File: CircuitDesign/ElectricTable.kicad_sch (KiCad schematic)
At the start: 7 parts

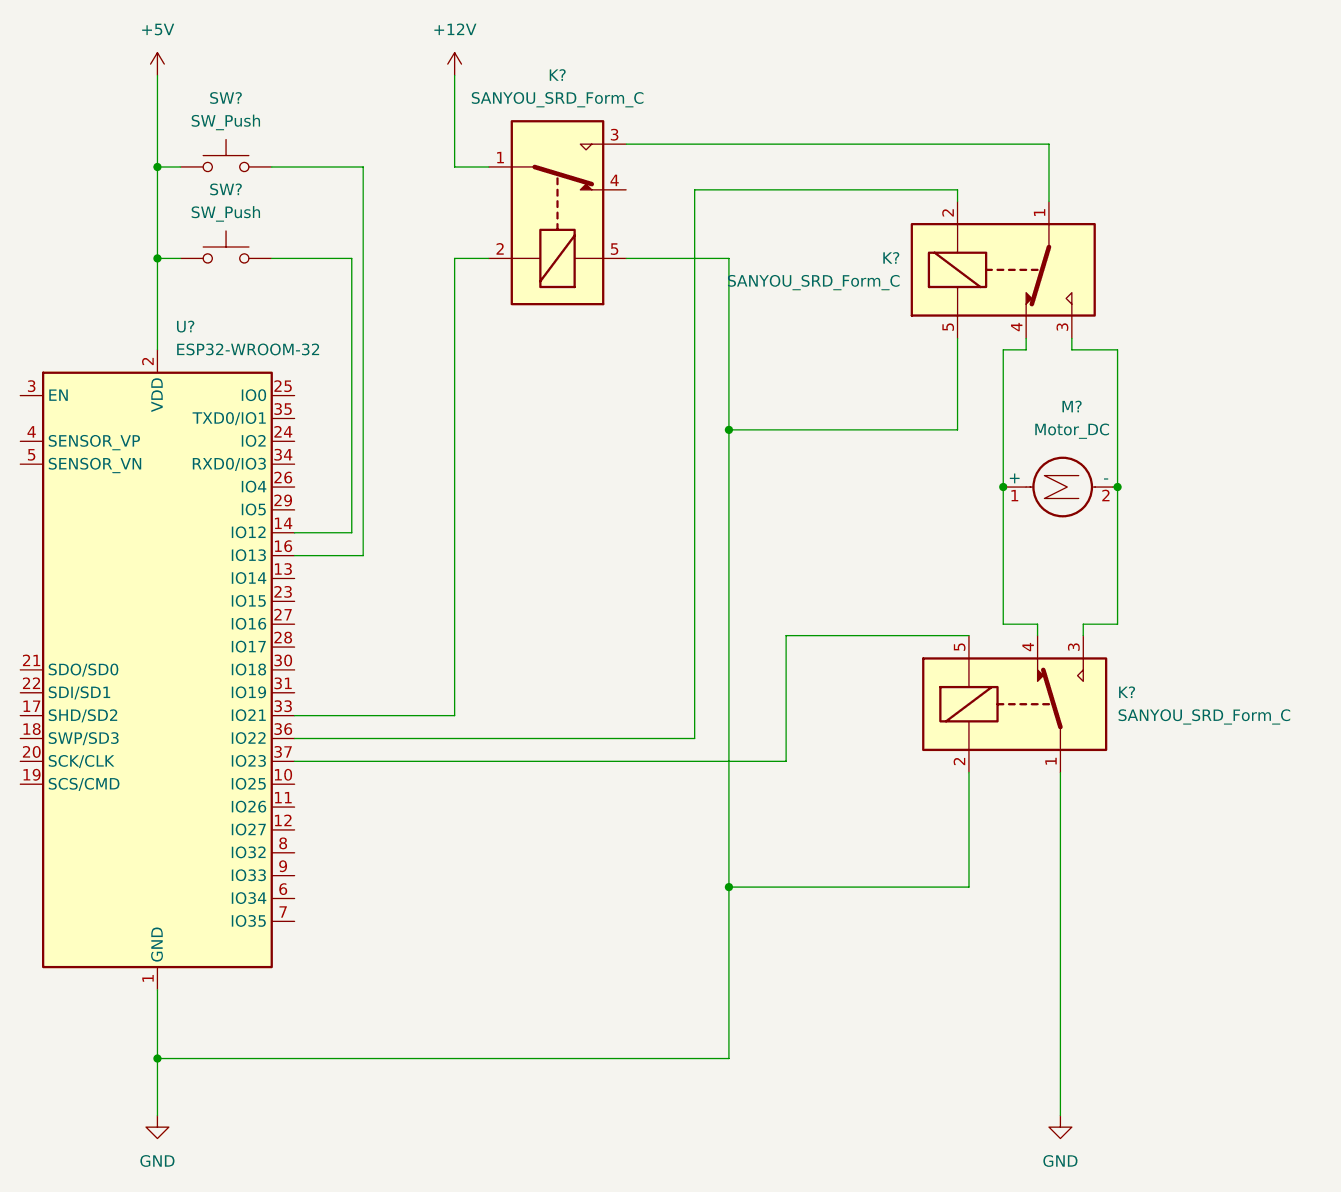
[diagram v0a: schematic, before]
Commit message: Simplified circuit to use dedicated H bridge instead of self made relay solution
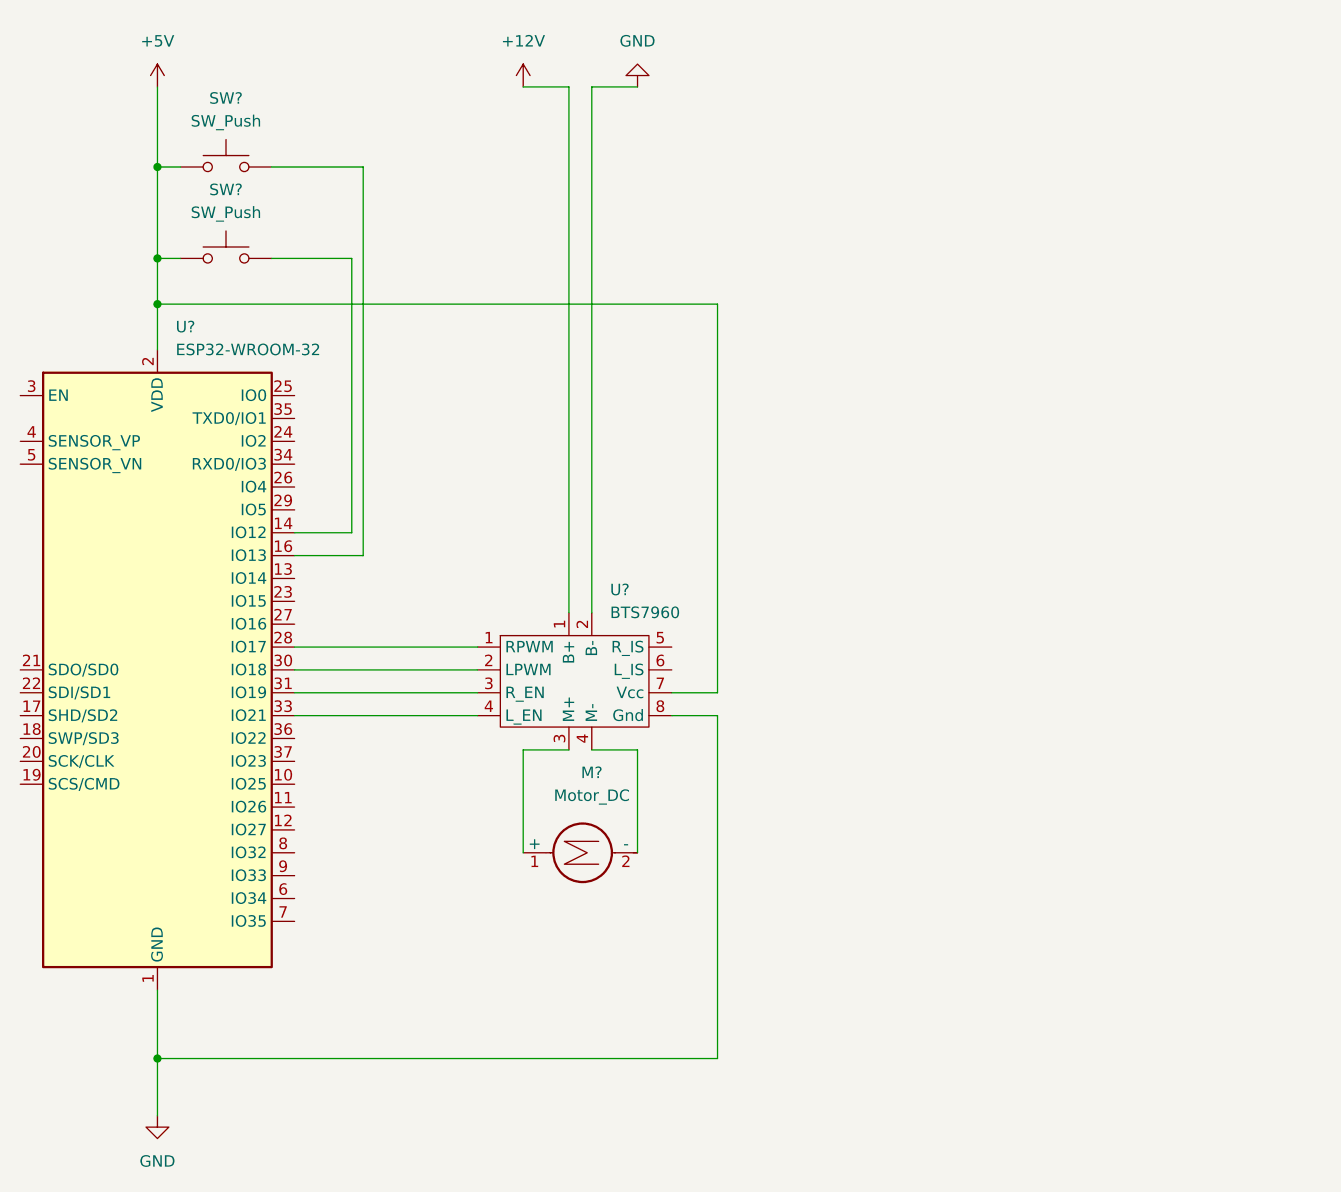
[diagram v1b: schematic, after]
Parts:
- removed K? (x3): SANYOU_SRD_Form_C, Relay_THT:Relay_SPDT_SANYOU_SRD_Series_Form_C, symbol Relay:SANYOU_SRD_Form_C
- added U?: BTS7960, symbol Power_Management:BTS7960
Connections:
- net +12V: now also U?.1 (RPWM)
- net +5V: now also U?.7 (Vcc)
- net GND: now also U?.2 (LPWM), U?.8 (Gnd)
- net at U?.28 (IO17): now also U?.1 (RPWM)
- net at U?.30 (IO18): now also U?.2 (LPWM)
- net at U?.31 (IO19): now also U?.3 (R_EN)
- net at U?.33 (IO21): now also U?.4 (M-)
- net at M?.2 (-): now also U?.4 (M-)
- net at M?.1 (+): now also U?.3 (R_EN)
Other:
- moved on the sheet: M?
